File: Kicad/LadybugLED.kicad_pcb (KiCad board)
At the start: 2 copper layers, 32.5 x 28.8 mm, 12 parts, among them P1 CONN_1, P2 CONN_1, P3 CONN_2, Q1 LB_MOS_N, U1 LB_MCP6241, U2 LB_7805

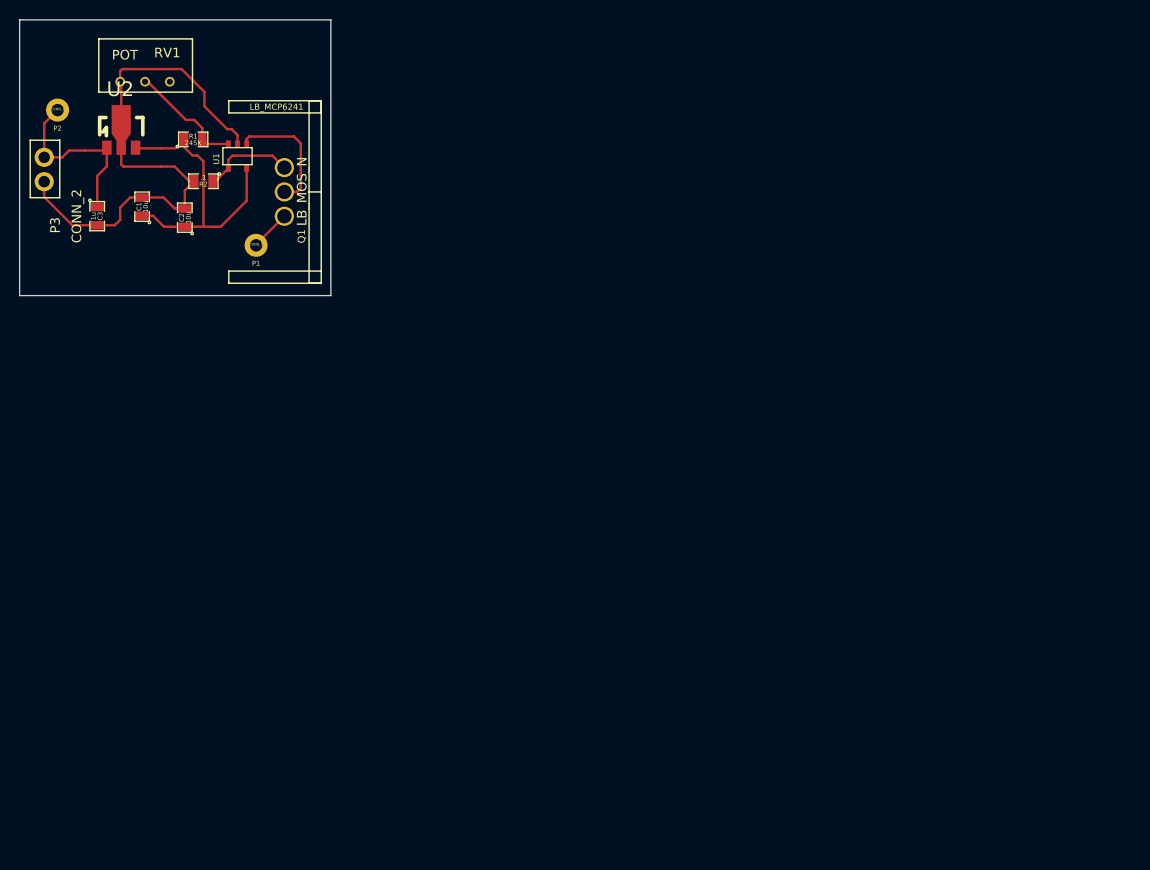
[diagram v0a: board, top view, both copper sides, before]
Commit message: buck regulator LED driver - first commit
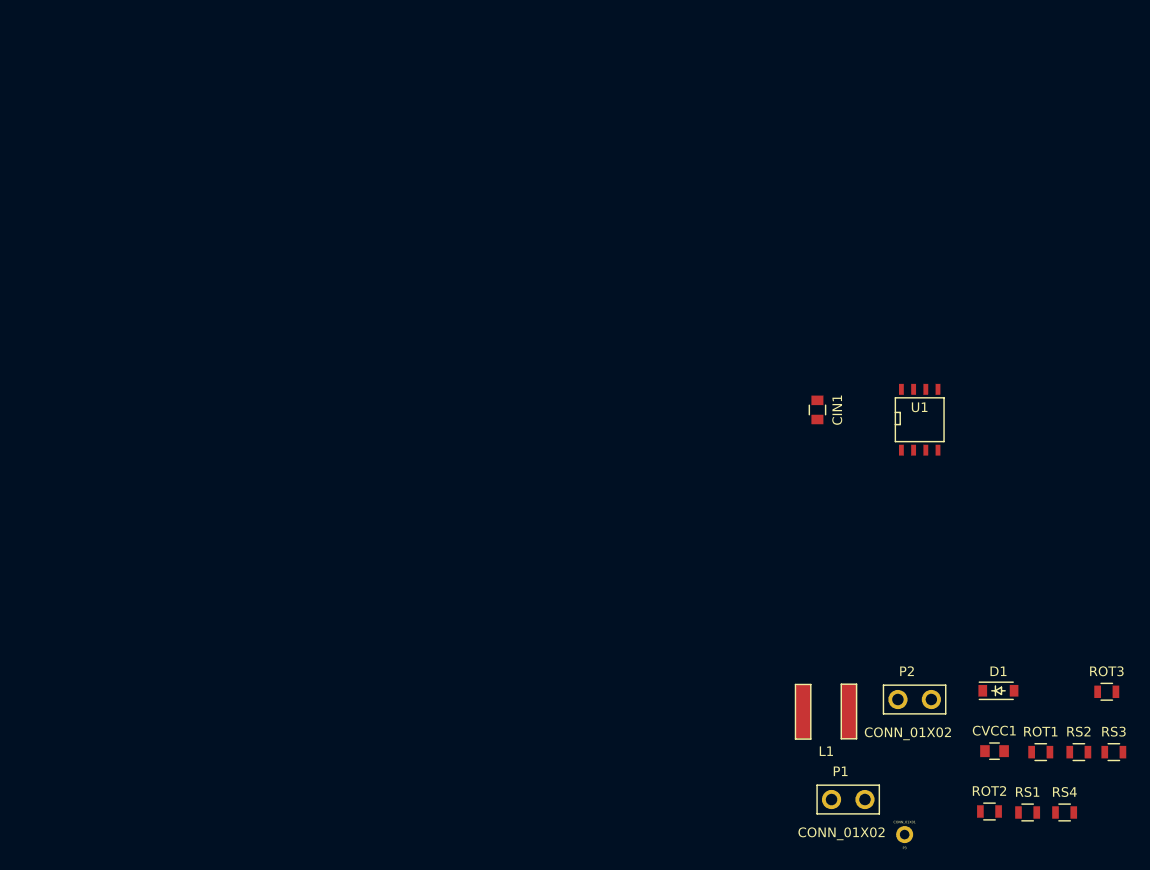
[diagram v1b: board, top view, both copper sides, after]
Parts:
- removed C1, C2: 10u, SM0805
- removed C3: 1u, SM0805
- removed Q1: LB_MOS_N, LB_LED_HEAT_SINK_MOSFET
- removed R1: 245K, SM0805
- removed R2: .1, SM0805
- removed RV1: POT, LB_POT
- removed U2: LB_7805, LB_SOT89_3
- added CIN1: 4.7µF, Capacitors_SMD:C_0805, F.Cu at (152.5, 79.6)
- added CVCC1: 1µ, Capacitors_SMD:C_0805, F.Cu at (171.0, 115.2)
- added D1: D_Schottky, Diodes_SMD:SOD-123, F.Cu at (171.4, 108.9)
- added L1: 47µ, LadybugHydro:L-NR6045T470M, F.Cu at (151.0, 108.4)
- added ROT1: 22K, Resistors_SMD:R_0805, F.Cu at (175.8, 115.3)
- added ROT2: 22K, Resistors_SMD:R_0805, F.Cu at (170.5, 121.5)
- added ROT3: 10K, Resistors_SMD:R_0805, F.Cu at (182.7, 109.0)
- added RS1: 1Ω, Resistors_SMD:R_0805, F.Cu at (174.5, 121.6)
- added RS2: 1Ω, Resistors_SMD:R_0805, F.Cu at (179.8, 115.3)
- added RS3: 1Ω, Resistors_SMD:R_0805, F.Cu at (183.5, 115.3)
- added RS4: 2.2Ω, Resistors_SMD:R_0805, F.Cu at (178.3, 121.6)
- P1, P2: value CONN_1 -> CONN_01X02; footprint LB_TestPoint -> LettuceBuddy:LB_CONN_2
- P3: value CONN_2 -> CONN_01X01; footprint LB_CONN_2 -> LettuceBuddy:LB_CONN_1
- U1: value LB_MCP6241 -> NCL30160; footprint SOT23-5 -> SMD_Packages:SOIC-8-N
- moved P3 112.7 mm to (161.6, 124.0), turned to 0 degrees
- moved P2 107.1 mm to (160.9, 109.9)
- moved P1 83.4 mm to (154.0, 120.3)
- moved U1 76.3 mm to (163.2, 80.7), turned to 0 degrees
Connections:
- P1 pad 1: /to_LED -> GND
- P2 pad 1: /9V -> Net-(CIN1-Pad1)
- P3 pad 1: /9V -> Net-(P3-Pad1)
- U1 pad 1: /Vout -> Net-(RS1-Pad2)
- U1 pad 2: GND -> Net-(RS1-Pad2)
- U1 pad 3: /Vin+ -> GND
- U1 pad 4: /Vin- -> Net-(CVCC1-Pad1)
- U1 pad 5: /5V -> Net-(ROT1-Pad1)
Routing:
- net GND: track 60.2 -> 0.00 mm
- net /5V: track 31.6 -> 0.00 mm
- net /9V: track 19.1 -> 0.00 mm
- net /Vout: track 13.1 -> 0.00 mm
- net /Vin+: track 12.1 -> 0.00 mm
- net /Vin-: track 9.64 -> 0.00 mm
- net /to_LED: track 4.25 -> 0.00 mm
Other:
- board outline removed
- net class Default: clearance 0.254 -> 0.2; trace_width 0.254 -> 0.25; via_dia 0.889 -> 0.6; via_drill 0.635 -> 0.4
- rule pad_to_mask_clearance: 0 -> 0.2
- rule trace_clearance: 0.254 -> 0.2
- rule trace_min: 0.254 -> 0.2
- rule via_min_drill: 0.508 -> 0.3
- rule via_min_size: 0.889 -> 0.4
